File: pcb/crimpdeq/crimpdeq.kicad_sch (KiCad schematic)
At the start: 47 parts, among them J2 USB4105-GF-A, Q1 SS8550, Q2 DMG3415U, U1 ESP32-C3-MINI-1, U2 MCP73831T-2ACI/OT, U3 HX711, U4 Rust_Board, U5 MAX17048G+T10, U6 SY8088

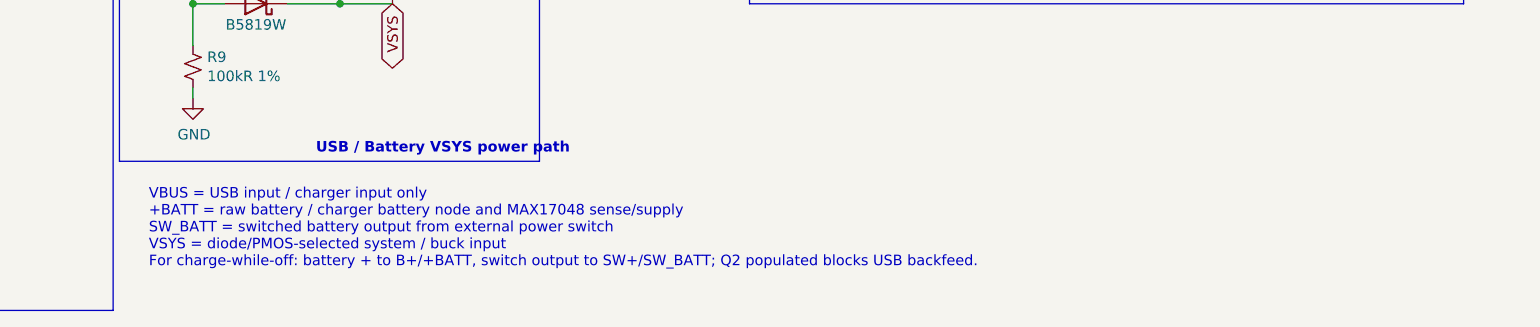
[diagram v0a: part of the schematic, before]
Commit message: feat: add battery negative pad
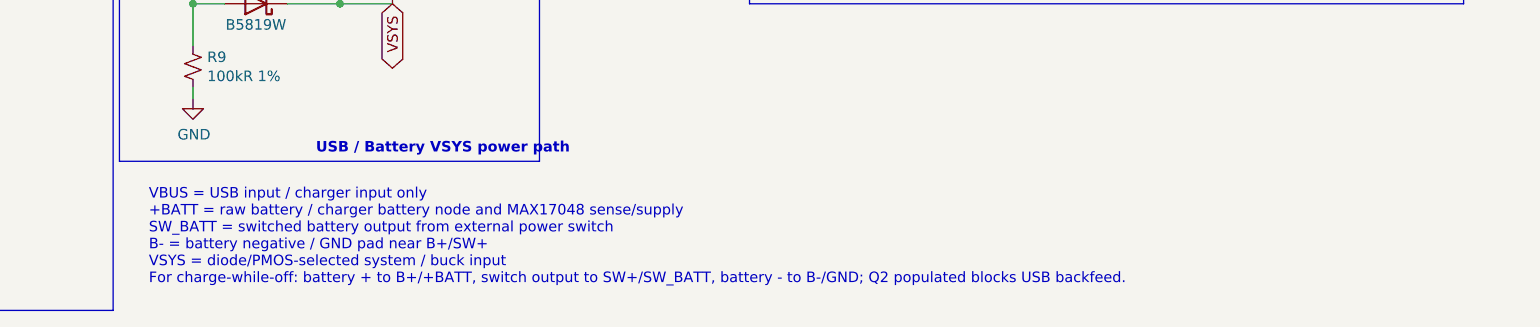
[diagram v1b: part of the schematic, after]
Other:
- note added: "VBUS = USB input / charger input only +BATT = raw battery / charger battery node and MAX17048 sense/supply SW_BATT = switched battery output from external power switch B- = battery negative / GND pad near B+/SW+ VSYS = diode/PMOS-selected system / buck input For charge-while-off: battery + to B+/+BATT, switch output to SW+/SW_BATT, battery - to B-/GND; Q2 populated blocks USB backfeed."
- note removed: "VBUS = USB input / charger input only +BATT = raw battery / charger battery node and MAX17048 sense/supply SW_BATT = switched battery output from external power switch VSYS = diode/PMOS-selected system / buck input For charge-while-off: battery + to B+/+BATT, switch output to SW+/SW_BATT; Q2 populated blocks USB backfeed."
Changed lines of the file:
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@@
 		)
 	)
-	(text "VBUS = USB input / charger input only\n+BATT = raw battery / charger battery node and MAX17048 sense/supply\nSW_BATT = switched battery output from external power switch\nVSYS = diode/PMOS-selected system / buck input\nFor charge-while-off: battery + to B+/+BATT, switch output to SW+/SW_BATT; Q2 populated blocks USB backfeed."
+	(text "VBUS = USB input / charger input only\n+BATT = raw battery / charger battery node and MAX17048 sense/supply\nSW_BATT = switched battery output from external power switch\nB- = battery negative / GND pad near B+/SW+\nVSYS = diode/PMOS-selected system / buck input\nFor charge-while-off: battery + to B+/+BATT, switch output to SW+/SW_BATT, battery - to B-/GND; Q2 populated blocks USB backfeed."
 		(exclude_from_sim no)
 		(at 125.476 182.372 0)

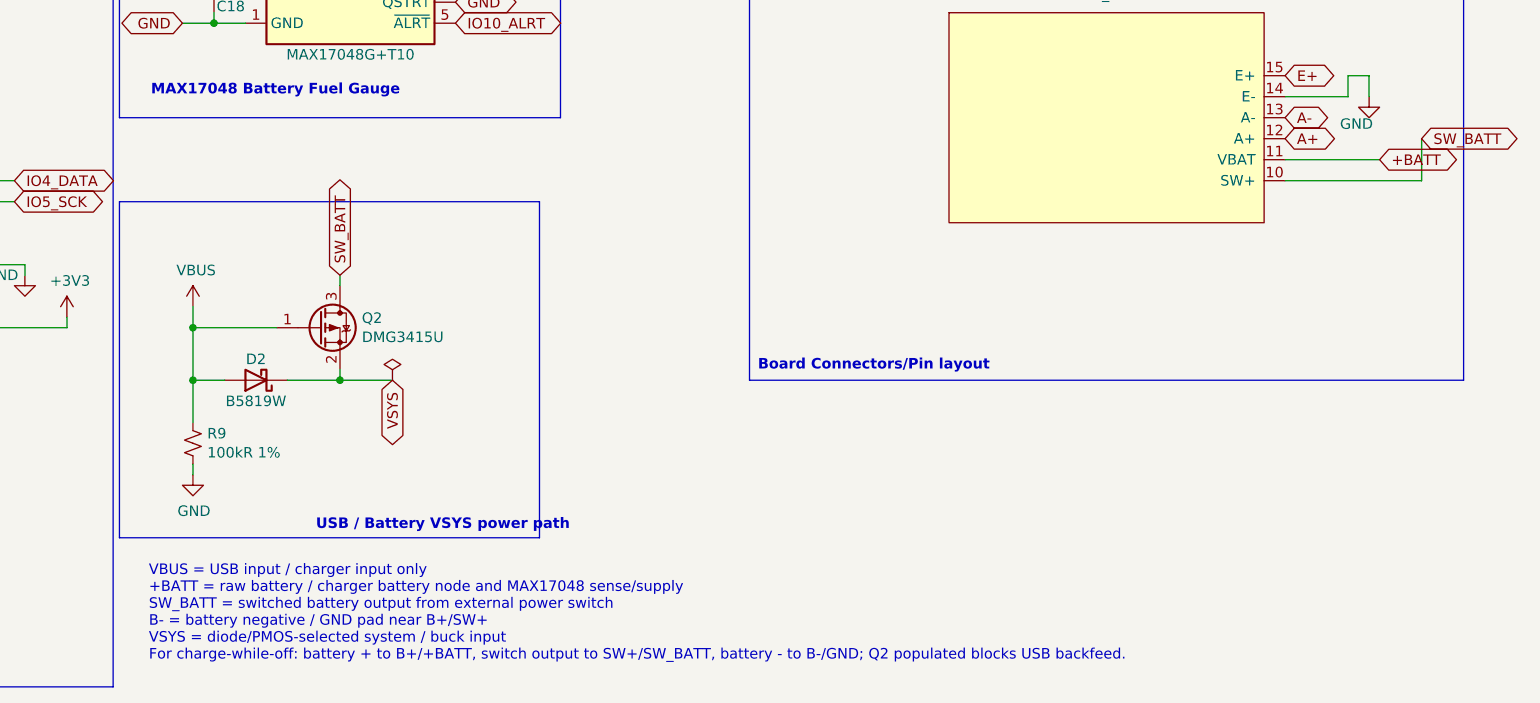
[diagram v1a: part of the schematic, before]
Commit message: docs: document battery connector pins
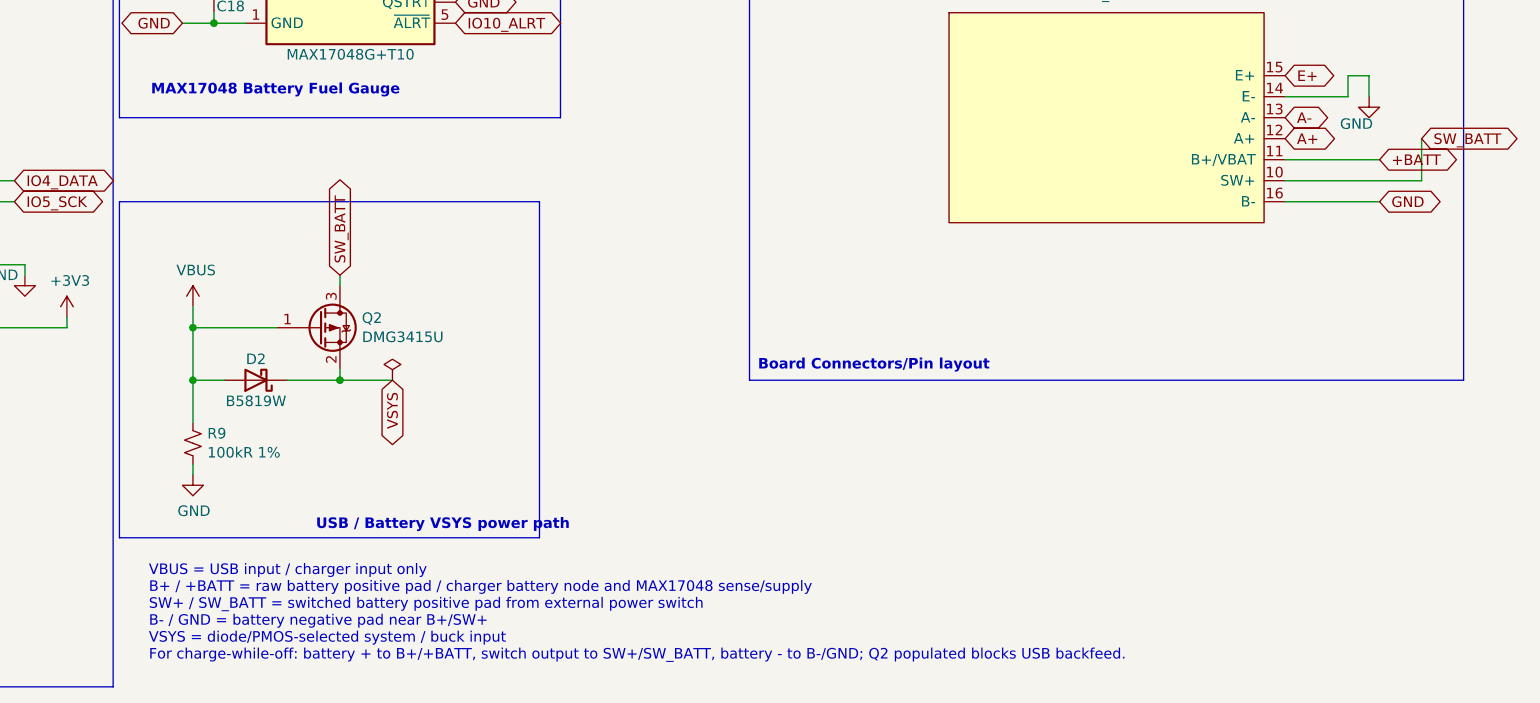
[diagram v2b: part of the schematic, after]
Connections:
- net GND: now also U4.16 (B-)
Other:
- note added: "VBUS = USB input / charger input only B+ / +BATT = raw battery positive pad / charger battery node and MAX17048 sense/supply SW+ / SW_BATT = switched battery positive pad from external power switch B- / GND = battery negative pad near B+/SW+ VSYS = diode/PMOS-selected system / buck input For charge-while-off: battery + to B+/+BATT, switch output to SW+/SW_BATT, battery - to B-/GND; Q2 populated b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"
- note removed: "VBUS = USB input / charger input only +BATT = raw battery / charger battery node and MAX17048 sense/supply SW_BATT = switched battery output from external power switch B- = battery negative / GND pad near B+/SW+ VSYS = diode/PMOS-selected system / buck input For charge-while-off: battery + to B+/+BATT, switch output to SW+/SW_BATT, battery - to B-/GND; Q2 populated blocks USB backfeed."
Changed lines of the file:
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@@
 		)
 	)
-	(text "VBUS = USB input / charger input only\n+BATT = raw battery / charger battery node and MAX17048 sense/supply\nSW_BATT = switched battery output from external power switch\nB- = battery negative / GND pad near B+/SW+\nVSYS = diode/PMOS-selected system / buck input\nFor charge-while-off: battery + to B+/+BATT, switch output to SW+/SW_BATT, battery - to B-/GND; Q2 populated blocks USB backfeed."
+	(text "VBUS = USB input / charger input only\nB+ / +BATT = raw battery positive pad / charger battery node and MAX17048 sense/supply\nSW+ / SW_BATT = switched battery positive pad from external power switch\nB- / GND = battery negative pad near B+/SW+\nVSYS = diode/PMOS-selected system / buck input\nFor charge-while-off: battery + to B+/+BATT, switch output to SW+/SW_BATT, battery - to B-/GND; Q2 populated blocks USB backfeed."
 		(exclude_from_sim no)
 		(at 125.476 182.372 0)
@@
 	(wire
 		(pts
+			(xy 262.89 138.43) (xy 274.32 138.43)
+		)
+		(stroke
+			(width 0)
+			(type default)
+		)
+	)
+	(wire
+		(pts
 			(xy 74.93 146.05) (xy 40.64 146.05)
 		)
@@
 		)
 	)
+	(global_label "GND"
+		(shape bidirectional)
+		(at 274.32 138.43 0)
+		(fields_autoplaced yes)
+		(effects
+			(font
+				(size 1.27 1.27)
+			)
+			(justify left)
+		)
+		(property "Intersheetrefs" "${INTERSHEET_REFS}"
+			(at 274.32 138.43 0)
+			(hide yes)
+			(show_name no)
+			(do_not_autoplace no)
+			(effects
+				(font
+					(size 1.27 1.27)
+				)
+				(justify left)
+			)
+		)
+	)
 	(global_label "A+"
 		(shape bidirectional)
@@
 		(pin "15"
 		)
+		(pin "16"
+		)
 		(instances

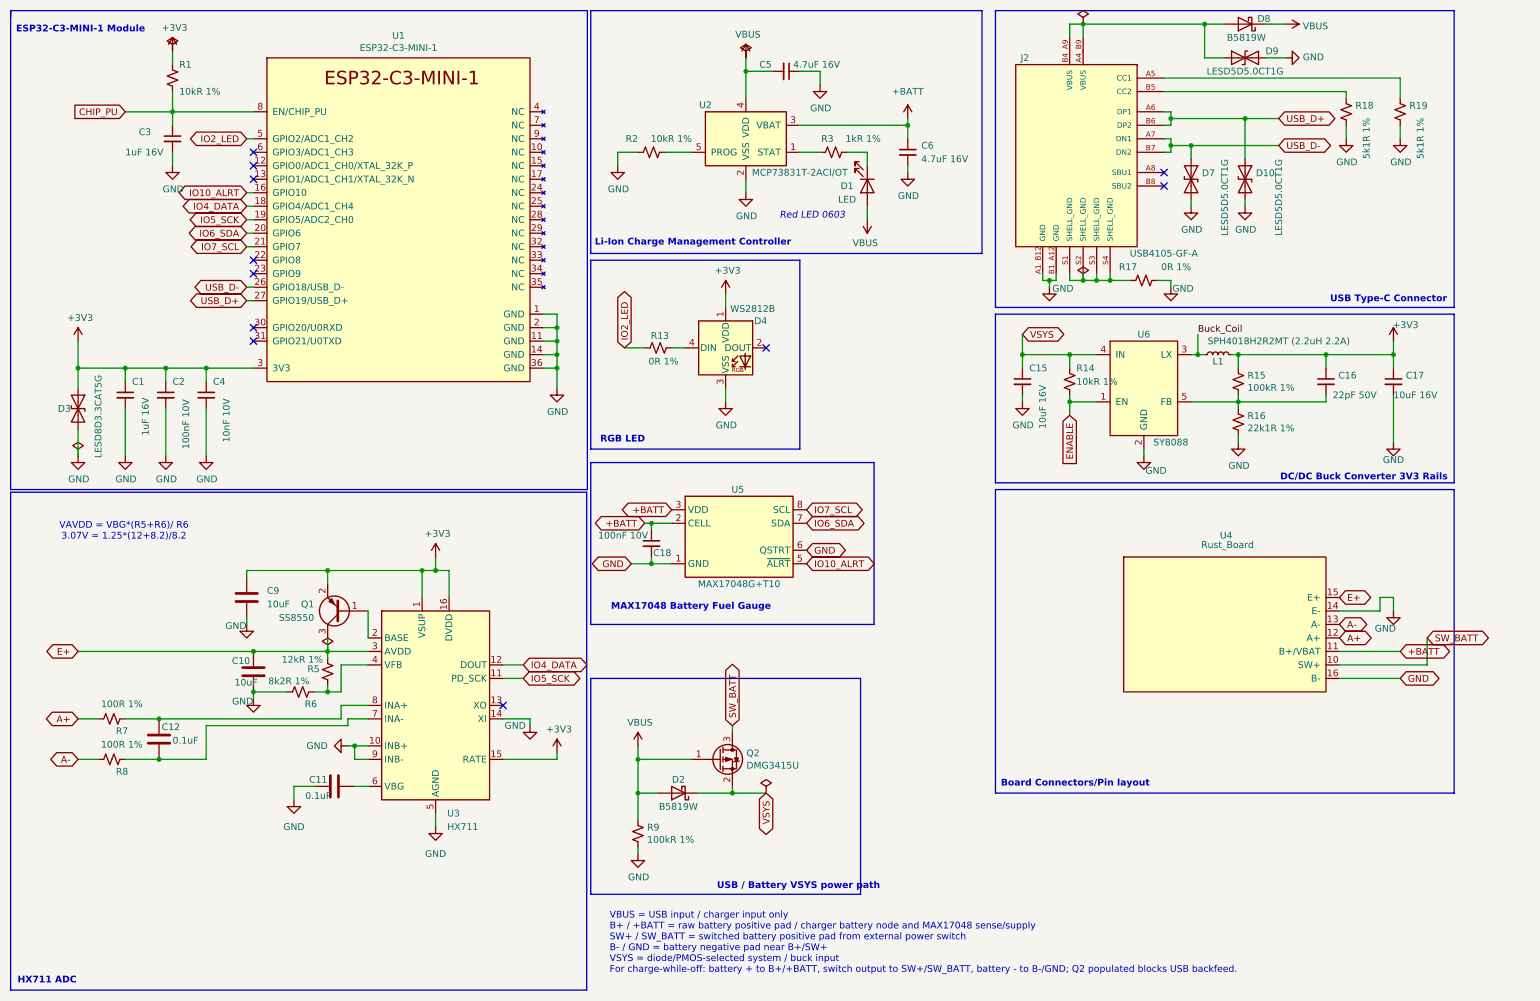
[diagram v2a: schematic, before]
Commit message: feat: link external pads to schematic
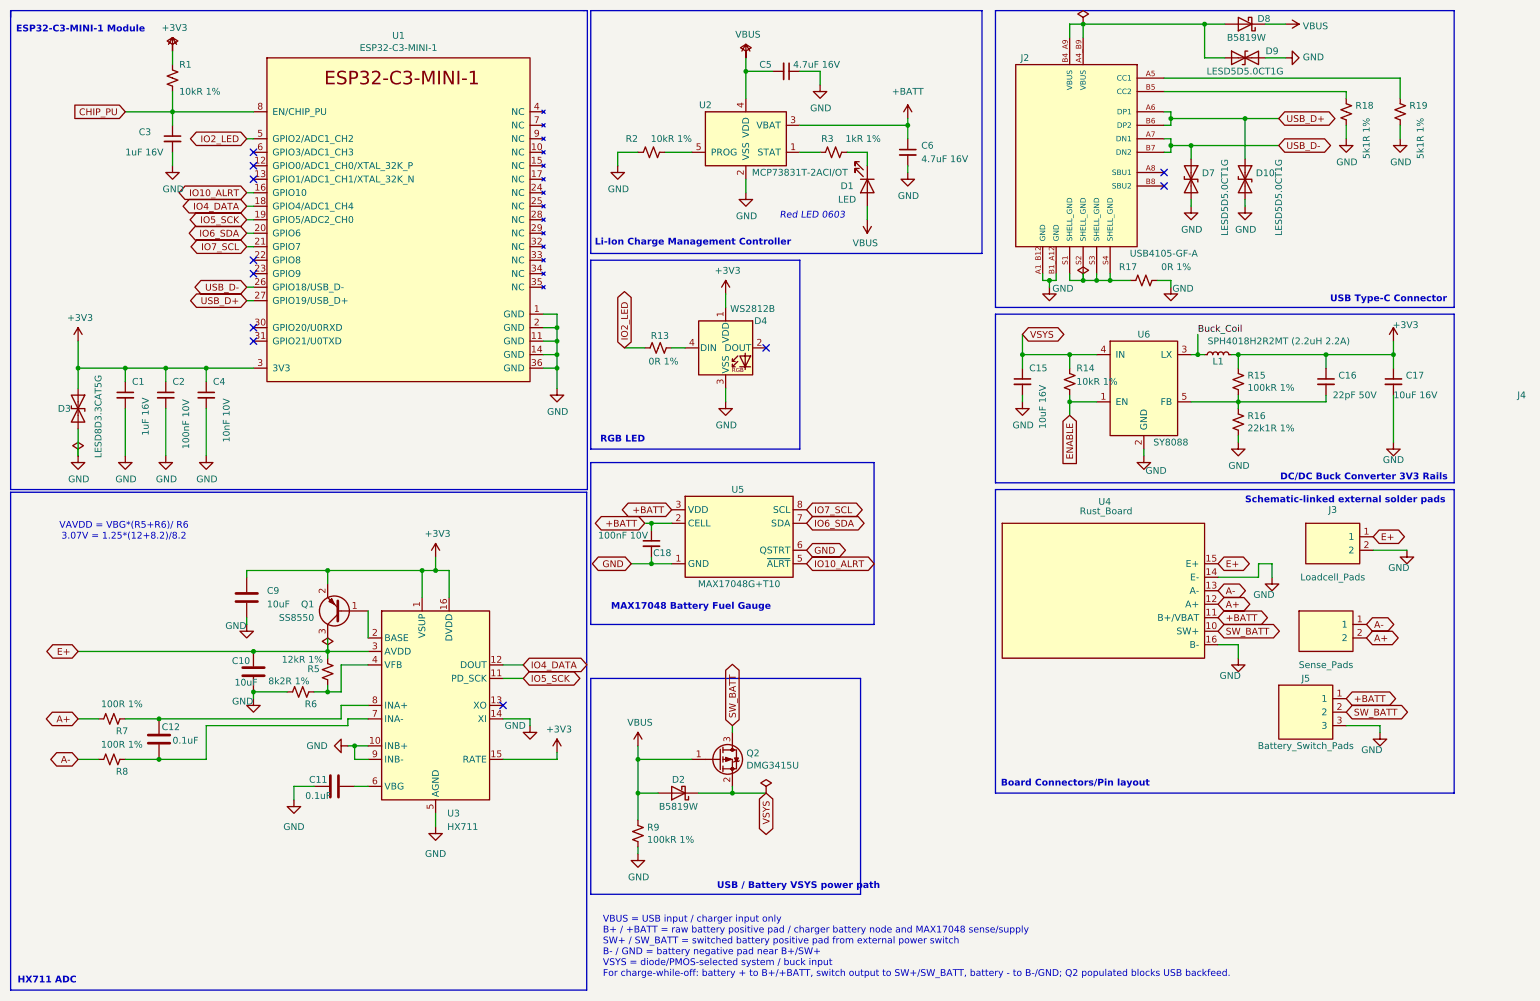
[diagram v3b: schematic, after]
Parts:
- added J3: Loadcell_Pads, External_Cable_Pads_Left, symbol Crimpdeq:External_Pads_2
- added J4: Sense_Pads, External_Sense_Pads_Right, symbol Crimpdeq:External_Pads_2
- added J5: Battery_Switch_Pads, External_Battery_Switch_Pads_Left, symbol Crimpdeq:External_Pads_3
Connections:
- net +BATT: now also J5.1
- net A+: now also J4.2
- net A-: now also J4.1
- net E+: now also J3.1
- net GND: now also J3.2, J5.3
- net SW_BATT: now also J5.2
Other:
- note added: "Schematic-linked external solder pads"
- moved on the sheet: U4
